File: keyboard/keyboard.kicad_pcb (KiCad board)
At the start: 2 copper layers, 214.3 x 140.5 mm, 133 parts, among them SW1 MX_SW_HS, SW10 MX_SW_HS, SW11 MX_SW_HS, SW12 MX_SW_HS, SW13 MX_SW_HS, SW14 MX_SW_HS, SW15 MX_SW_HS, SW16 MX_SW_HS, SW17 MX_SW_HS, SW18 MX_SW_HS, SW19 MX_SW_HS, SW2 MX_SW_HS, SW20 MX_SW_HS, SW21 MX_SW_HS, SW22 MX_SW_HS, SW23 MX_SW_HS, SW24 MX_SW_HS, SW25 MX_SW_HS, SW26 MX_SW_HS, SW27 MX_SW_HS, SW28 MX_SW_HS, SW29 MX_SW_HS, SW3 MX_SW_HS, SW30 MX_SW_HS, SW31 MX_SW_HS, SW32 MX_SW_HS, SW33 MX_SW_HS, SW34 MX_SW_HS, SW35 MX_SW_HS, SW36 MX_SW_HS, SW37 MX_SW_HS, SW38 MX_SW_HS, SW39 MX_SW_HS, SW4 MX_SW_HS, SW40 MX_SW_HS, SW41 MX_SW_HS, SW42 MX_SW_HS, SW43 MX_SW_HS, SW44 MX_SW_HS, SW45 MX_SW_HS, SW46 MX_SW_HS, SW47 MX_SW_HS, SW48 MX_SW_HS, SW49 MX_SW_HS, SW5 MX_SW_HS, SW50 MX_SW_HS, SW51 MX_SW_HS, SW52 MX_SW_HS, SW53 MX_SW_HS, SW54 MX_SW_HS, SW55 MX_SW_HS, SW56 MX_SW_HS, SW57 MX_SW_HS, SW58 MX_SW_HS, SW59 MX_SW_HS, SW6 MX_SW_HS, SW60 MX_SW_HS, SW61 MX_SW_HS, SW62 MX_SW_HS, SW63 MX_SW_HS, SW64 MX_SW_HS, SW7 MX_SW_HS, SW8 MX_SW_HS, SW9 MX_SW_HS, U1 ProMicro

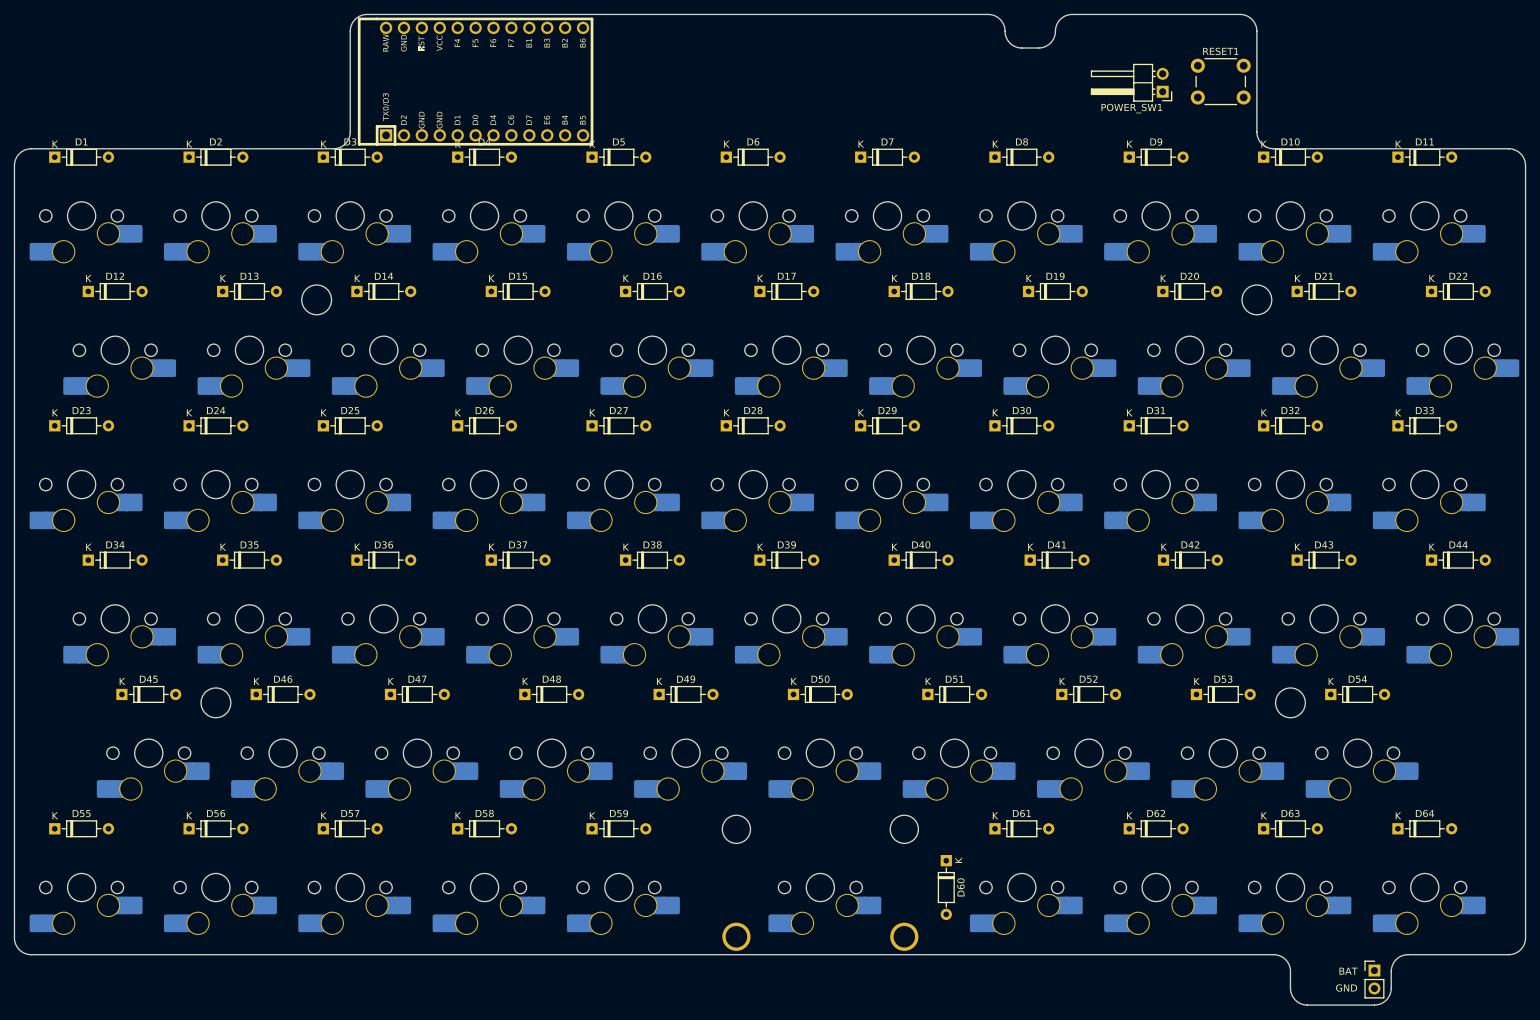
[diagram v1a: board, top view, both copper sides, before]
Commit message: Adjust the placement of the nicenano to align the USB-C port.
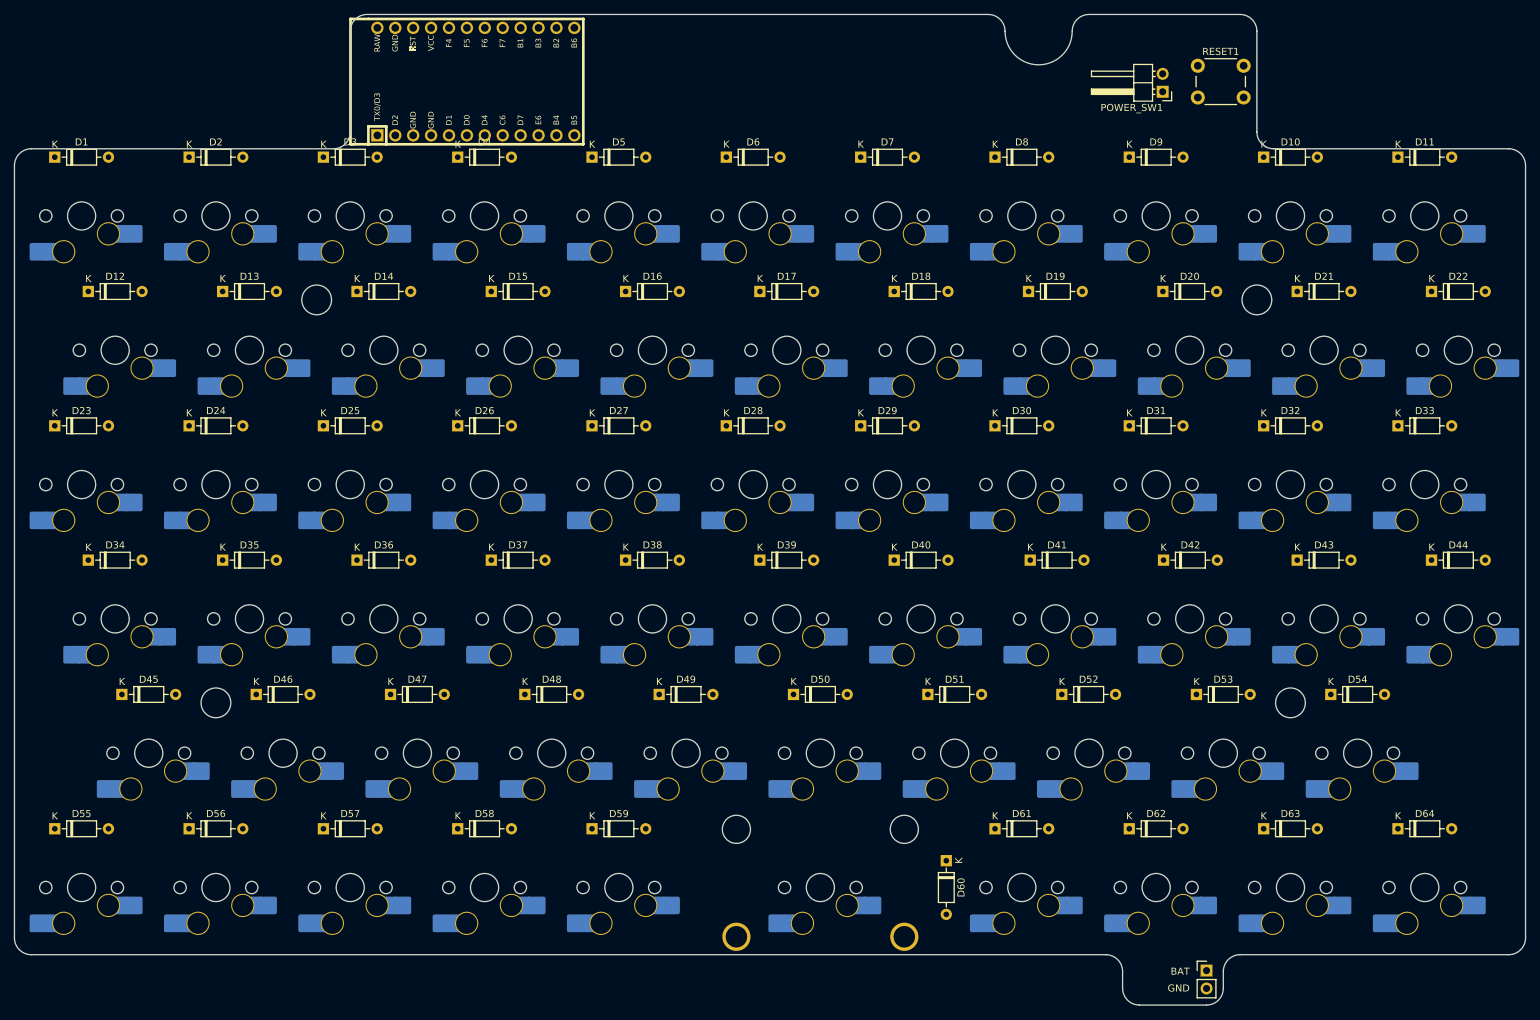
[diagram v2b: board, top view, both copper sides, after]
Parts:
- moved BATTERY1 23.8 mm to (209.6, 149.9)
- moved U1 1.23 mm to (105.9, 23.8)
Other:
- outline, holes or cut-outs redrawn
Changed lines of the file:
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@@
     (fp_line (start 9.03125 8.000001) (end 14.78125 8.000001) (layer "Eco2.User") (width 0.05))
     (fp_arc (start -15.28125 -5.499999) (mid -15.134803 -5.853552) (end -14.78125 -5.999999) (layer "Eco2.User") (width 0.05))
-    (fp_arc (start 15.28125 7.500001) (mid 15.134806 7.853571) (end 14.78125 8.000001) (layer "Eco2.User") (width 0.05))
+    (fp_arc (start 15.28125 7.500001) (mid 15.1348 7.853536) (end 14.78125 8.000001) (layer "Eco2.User") (width 0.05))
     (fp_arc (start -14.78125 8.000001) (mid -15.134803 7.853554) (end -15.28125 7.500001) (layer "Eco2.User") (width 0.05))
     (fp_arc (start -8.53125 7.500001) (mid -8.677697 7.853554) (end -9.03125 8.000001) (layer "Eco2.User") (width 0.05))
     (fp_arc (start 8.53125 -5.499999) (mid 8.677685 -5.853565) (end 9.03125 -5.999999) (layer "Eco2.User") (width 0.05))
-    (fp_arc (start 14.780039 -5.999999) (mid 15.133567 -5.853539) (end 15.280039 -5.499999) (layer "Eco2.User") (width 0.05))
+    (fp_arc (start 14.780039 -5.999999) (mid 15.133602 -5.853545) (end 15.280039 -5.499999) (layer "Eco2.User") (width 0.05))
     (fp_arc (start -9.03125 -5.999999) (mid -8.677697 -5.853552) (end -8.53125 -5.499999) (layer "Eco2.User") (width 0.05))
-    (fp_arc (start 9.03125 8.000001) (mid 8.677729 7.853537) (end 8.53125 7.500001) (layer "Eco2.User") (width 0.05))
+    (fp_arc (start 9.03125 8.000001) (mid 8.677693 7.853543) (end 8.53125 7.500001) (layer "Eco2.User") (width 0.05))
     (pad "" thru_hole circle (at -11.90625 -6.985 180) (size 4 4) (drill 3.048) (layers *.Cu "B.Mask"))
     (pad "" np_thru_hole circle (at -11.90625 8.255 180) (size 3.9878 3.9878) (drill 3.9878) (layers *.Cu *.Mask))
@@
   )
   (footprint "Connector_PinHeader_2.54mm:PinHeader_1x02_P2.54mm_Vertical" (layer "F.Cu")
-    (at 233.3625 149.89)
+    (at 209.55 149.89)
     (descr "Through hole straight pin header, 1x02, 2.54mm pitch, single row")
     (tags "Through hole pin header THT 1x02 2.54mm single row")
@@
   )
   (footprint "Keebio-Parts:ArduinoProMicro" (layer "F.Cu")
-    (at 107.15625 23.8125)
+    (at 105.92225 23.8125)
     (property "Sheetfile" "keyboard.kicad_sch")
     (property "Sheetname" "")
@@
   (gr_line (start 216.69375 30.95625) (end 216.69375 16.66875) (layer "Edge.Cuts") (width 0.1))
   (gr_circle (center 221.45625 111.91875) (end 223.56625 111.91875) (layer "Edge.Cuts") (width 0.1) (fill none))
-  (gr_line (start 252.4125 147.6375) (end 238.125 147.6375) (layer "Edge.Cuts") (width 0.1))
-  (gr_arc (start 235.74375 150.01875) (mid 236.441202 148.334952) (end 238.125 147.6375) (layer "Edge.Cuts") (width 0.1))
+  (gr_line (start 252.4125 147.6375) (end 214.3125 147.6375) (layer "Edge.Cuts") (width 0.1))
+  (gr_arc (start 211.93125 150.01875) (mid 212.628702 148.334952) (end 214.3125 147.6375) (layer "Edge.Cuts") (width 0.1))
   (gr_line (start 254.79375 145.25625) (end 254.79375 35.71875) (layer "Edge.Cuts") (width 0.1))
-  (gr_line (start 233.3625 154.78125) (end 223.8375 154.78125) (layer "Edge.Cuts") (width 0.1))
-  (gr_arc (start 188.11875 16.66875) (mid 188.816202 14.984952) (end 190.5 14.2875) (layer "Edge.Cuts") (width 0.1))
+  (gr_line (start 209.55 154.78125) (end 200.025 154.78125) (layer "Edge.Cuts") (width 0.1))
+  (gr_arc (start 190.5 16.66875) (mid 191.197452 14.984952) (end 192.88125 14.2875) (layer "Edge.Cuts") (width 0.1))
   (gr_arc (start 252.4125 33.3375) (mid 254.096269 34.034981) (end 254.79375 35.71875) (layer "Edge.Cuts") (width 0.1))
   (gr_arc (start 178.59375 14.2875) (mid 180.277548 14.984952) (end 180.975 16.66875) (layer "Edge.Cuts") (width 0.1))
   (gr_circle (center 69.05625 111.91875) (end 71.16625 111.91875) (layer "Edge.Cuts") (width 0.1) (fill none))
-  (gr_line (start 42.8625 147.6375) (end 219.075 147.6375) (layer "Edge.Cuts") (width 0.1))
-  (gr_arc (start 235.74375 152.4) (mid 235.046298 154.083798) (end 233.3625 154.78125) (layer "Edge.Cuts") (width 0.1))
+  (gr_line (start 42.8625 147.6375) (end 195.2625 147.6375) (layer "Edge.Cuts") (width 0.1))
+  (gr_arc (start 211.93125 152.4) (mid 211.233798 154.083798) (end 209.55 154.78125) (layer "Edge.Cuts") (width 0.1))
   (gr_arc (start 254.79375 145.25625) (mid 254.096269 146.940019) (end 252.4125 147.6375) (layer "Edge.Cuts") (width 0.1))
   (gr_arc (start 40.48125 35.71875) (mid 41.178717 34.034967) (end 42.8625 33.3375) (layer "Edge.Cuts") (width 0.1))
@@
   (gr_line (start 85.725 33.3375) (end 42.8625 33.3375) (layer "Edge.Cuts") (width 0.1))
   (gr_arc (start 214.3125 14.2875) (mid 215.996298 14.984952) (end 216.69375 16.66875) (layer "Edge.Cuts") (width 0.1))
-  (gr_arc (start 223.8375 154.78125) (mid 222.153702 154.083798) (end 221.45625 152.4) (layer "Edge.Cuts") (width 0.1))
-  (gr_arc (start 183.35625 19.05) (mid 181.672452 18.352548) (end 180.975 16.66875) (layer "Edge.Cuts") (width 0.1))
-  (gr_line (start 185.7375 19.05) (end 183.35625 19.05) (layer "Edge.Cuts") (width 0.1))
-  (gr_line (start 221.45625 152.4) (end 221.45625 150.01875) (layer "Edge.Cuts") (width 0.1))
-  (gr_arc (start 188.11875 16.66875) (mid 187.421298 18.352548) (end 185.7375 19.05) (layer "Edge.Cuts") (width 0.1))
+  (gr_arc (start 200.025 154.78125) (mid 198.341202 154.083798) (end 197.64375 152.4) (layer "Edge.Cuts") (width 0.1))
+  (gr_line (start 197.64375 152.4) (end 197.64375 150.01875) (layer "Edge.Cuts") (width 0.1))
+  (gr_arc (start 190.5 16.66875) (mid 185.7375 21.43125) (end 180.975 16.66875) (layer "Edge.Cuts") (width 0.1))
   (gr_arc (start 42.8625 147.6375) (mid 41.178731 146.940019) (end 40.48125 145.25625) (layer "Edge.Cuts") (width 0.1))
-  (gr_arc (start 219.075 147.6375) (mid 220.758798 148.334952) (end 221.45625 150.01875) (layer "Edge.Cuts") (width 0.1))
-  (gr_line (start 235.74375 150.01875) (end 235.74375 152.4) (layer "Edge.Cuts") (width 0.1))
-  (gr_line (start 190.5 14.2875) (end 214.3125 14.2875) (layer "Edge.Cuts") (width 0.1))
+  (gr_arc (start 195.2625 147.6375) (mid 196.946298 148.334952) (end 197.64375 150.01875) (layer "Edge.Cuts") (width 0.1))
+  (gr_line (start 211.93125 150.01875) (end 211.93125 152.4) (layer "Edge.Cuts") (width 0.1))
+  (gr_line (start 192.88125 14.2875) (end 214.3125 14.2875) (layer "Edge.Cuts") (width 0.1))
   (gr_arc (start 219.075 33.3375) (mid 217.391202 32.640048) (end 216.69375 30.95625) (layer "Edge.Cuts") (width 0.1))
   (gr_line (start 219.075 33.3375) (end 252.4125 33.3375) (layer "Edge.Cuts") (width 0.1))
-  (gr_text "GND" (at 230.98125 152.4) (layer "F.SilkS")
+  (gr_text "GND" (at 207.16875 152.4) (layer "F.SilkS")
     (effects (font (size 1 1) (thickness 0.15)) (justify right))
   )
-  (gr_text "BAT" (at 230.98125 150.01875) (layer "F.SilkS")
+  (gr_text "BAT" (at 207.16875 150.01875) (layer "F.SilkS")
     (effects (font (size 1 1) (thickness 0.15)) (justify right))
   )
